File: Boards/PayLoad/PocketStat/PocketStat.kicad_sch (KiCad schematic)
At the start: 71 parts, among them J20 DX07S016JA1R1500, J3 MEM2061-01-188-00-A_REVA, J5 BM03B-SRSS-TBLFSN, Q1 BC857CMB_315, U1 HDC2080DMBR, U4 LPS22DFTR, U5 W25Q128JVSIQ TR, U6 BMP581, U8 ST1L05APU33R

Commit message: PocketStat update
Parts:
- removed R1, R2: 2k, Resistor-0402:RES_0402, symbol Device:R
- added R26, R27: 2k, Resistor-0402:RES_0402, symbol Device:R
- U4: footprint QFN_22DFTR_STM -> BARO LPS22DFTR:QFN_22DFTR_STM
- U6: footprint QFN10_BMP581_BOS -> BARO BMP581:QFN10_BMP581_BOS
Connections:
- net +3.3V: now also U4.6 (CS), R26.1, R27.1; no longer HM1.2 (~{CS})
- net BAR1 RDY: now also MCU2.2 (GPIO0); no longer MCU2.6 (GPIO4)
- net BAR2 RDY: now also MCU2.32 (GPIO21); no longer MCU2.15 (GPIO12)
- net GND: now also U4.5 (SDO/SA0), U6.5 (SDO); no longer HM1.5 (SDO)
- net Humidity RDY: now also MCU2.38 (GPIO26_ADC0); no longer MCU2.35 (GPIO23)
- net LED Status: now also MCU2.18 (GPIO15); no longer MCU2.31 (GPIO20)
- net MISO1 SPI: now also HM1.5 (SDO); no longer U4.5 (SDO/SA0), U6.5 (SDO)
- net MOSI1 SPI: now also HM1.3 (SDI); no longer U4.4 (SDA/SDI/SDISDO), U6.4 (SDI)
- net SCK1 SPI: now also HM1.4 (SCK); no longer U4.2 (SCK), U6.2 (SCK)
- net SCL0 I2C: now also U6.2 (SCK)
- net SCL1 I2C: now also U4.2 (SCK), R27.2; no longer HM1.4 (SCK)
- net SDA0 I2C: now also U6.4 (SDI)
- net SDA1 I2C: now also U4.4 (SDA/SDI/SDISDO), R26.2; no longer HM1.3 (SDI)
- net BAR1 ~{CS} SPI renamed HUM ~{CS} SPI
- net HUM ~{CS} SPI: now also HM1.2 (~{CS}); no longer U4.6 (CS)
- net BAR2 ~{CS} SPI: no longer names the net of U6.6 (CSB)
- net BAR2 ~{CS} SPI: no longer MCU2.16 (GPIO13)
- no-connect marks 19 -> 21
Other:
- note added: "BOSH BMP581: 400Hz, I2C ADDR 0x46 ST LPS22DF: 200Hz, I2C ADDR 0x5C"
- note added: "Bosh BME280: 1Hz Texas HDC2080: 1Hz, I2C ADDR 0x41"
- note removed: "Bosh BME280: 1Hz, I2C ADDR 0x76 Texas HDC2080: 1Hz, I2C ADDR 0x41"
- note removed: "ST LPS22DF 200Hz BOSH BMP581: 400Hz"
- moved on the sheet: C1, C13, C2, C28, C3, C4, C5, HM1, R17, R18, U1, U4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

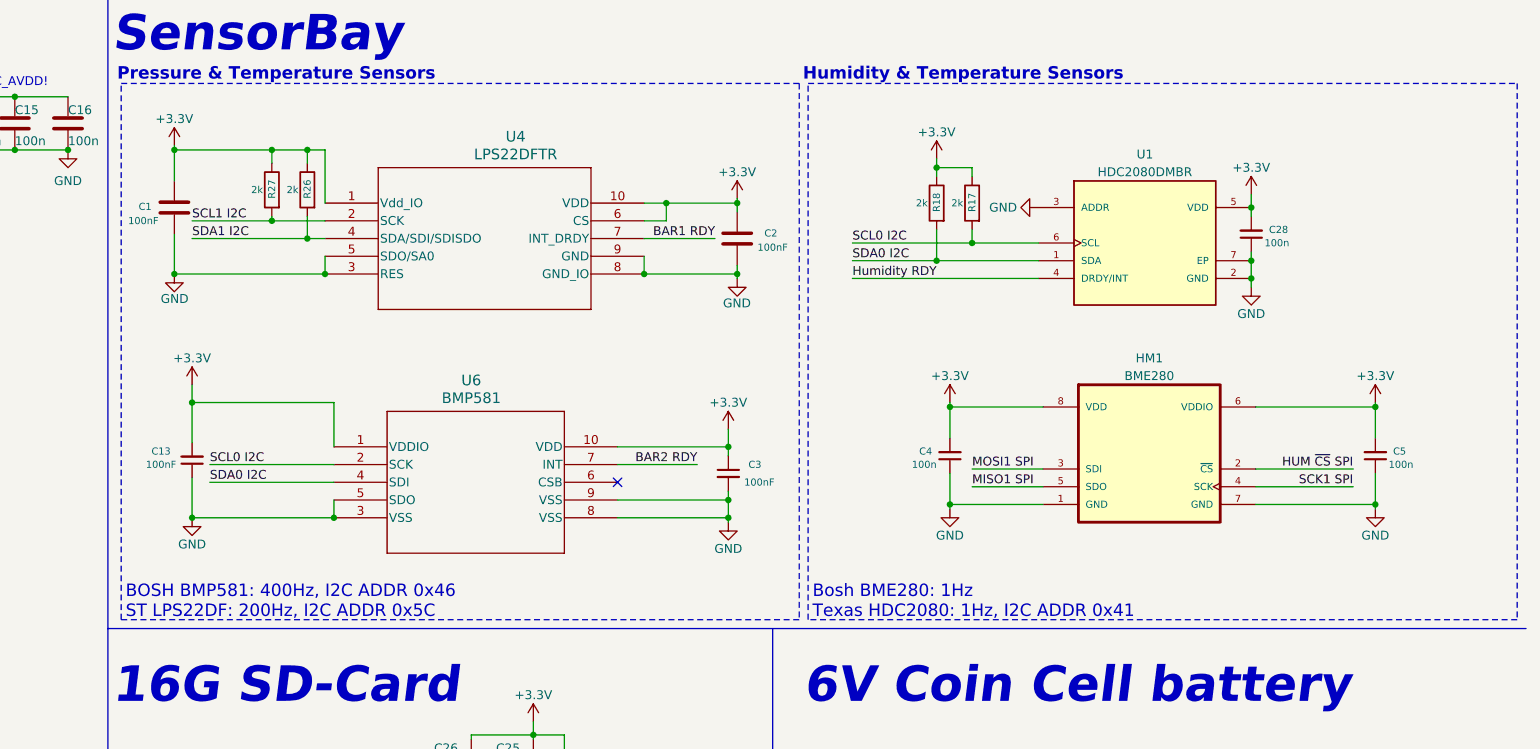
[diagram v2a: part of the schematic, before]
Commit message: Pocket Stat Schematic Notation Update
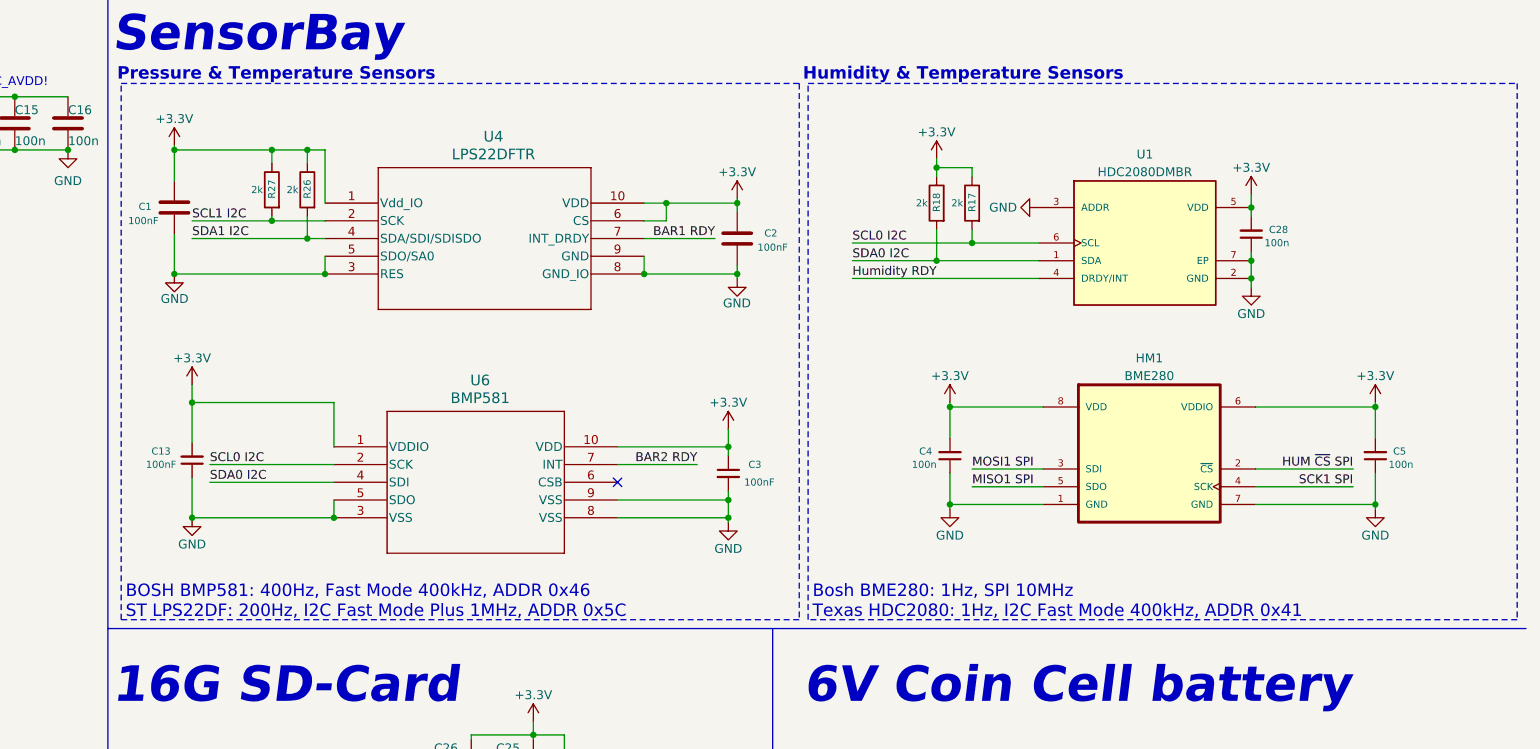
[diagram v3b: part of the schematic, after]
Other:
- note added: "BOSH BMP581: 400Hz, Fast Mode 400kHz, ADDR 0x46 ST LPS22DF: 200Hz, I2C Fast Mode Plus 1MHz, ADDR 0x5C"
- note added: "Bosh BME280: 1Hz, SPI 10MHz Texas HDC2080: 1Hz, I2C Fast Mode 400kHz, ADDR 0x41"
- note removed: "BOSH BMP581: 400Hz, I2C ADDR 0x46 ST LPS22DF: 200Hz, I2C ADDR 0x5C"
- note removed: "Bosh BME280: 1Hz Texas HDC2080: 1Hz, I2C ADDR 0x41"
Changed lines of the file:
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@@
 		)
 	)
-	(text "BOSH BMP581: 400Hz, I2C ADDR 0x46\nST LPS22DF: 200Hz, I2C ADDR 0x5C\n"
+	(text "BOSH BMP581: 400Hz, Fast Mode 400kHz, ADDR 0x46\nST LPS22DF: 200Hz, I2C Fast Mode Plus 1MHz, ADDR 0x5C\n"
 		(exclude_from_sim no)
 		(at 142.875 100.965 0)
@@
 		)
 	)
-	(text "Bosh BME280: 1Hz\nTexas HDC2080: 1Hz, I2C ADDR 0x41"
+	(text "Bosh BME280: 1Hz, SPI 10MHz\nTexas HDC2080: 1Hz, I2C Fast Mode 400kHz, ADDR 0x41"
 		(exclude_from_sim no)
 		(at 241.3 100.965 0)
@@
 		(dnp no)
 		(property "Reference" "U6"
-			(at 192.405 69.215 0)
+			(at 193.675 69.215 0)
 			(effects
 				(font
@@
 		)
 		(property "Value" "BMP581"
-			(at 192.405 71.755 0)
+			(at 193.675 71.755 0)
 			(effects
 				(font
@@
 		(dnp no)
 		(property "Reference" "U4"
-			(at 198.755 34.29 0)
+			(at 195.58 34.29 0)
 			(effects
 				(font
@@
 		)
 		(property "Value" "LPS22DFTR"
-			(at 198.755 36.83 0)
+			(at 195.58 36.83 0)
 			(effects
 				(font

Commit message: pocketstat power update
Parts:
- removed D1, D2: RSX301L-30DDTE25, Diode-Schottky_RSX301L:DIOM5026X220N, symbol RSX301L-30DDTE25:RSX301L-30DDTE25
- added D1, D2: PMEG2010ER, Diode-Schottky_PMEG2010ER:SODFL3517X110N, symbol PMEG2010ER:PMEG2010ER
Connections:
- net VBUS: now also D1.A
- net at JP6.1 (A): now also D2.A
- net +6V renamed +5V
- net +5V: now also D1.C, D2.C
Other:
- note added: "USB-C MUST BE DISCONNECTED WHEN BATTERY JUMPER IS SHORTED"
- moved on the sheet: BT1, C27, C36, C6, JP6

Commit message: update
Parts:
- C6: value 4.7u -> 1u
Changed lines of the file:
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@@
 			)
 		)
-		(property "Value" "4.7u"
+		(property "Value" "1u"
 			(at 262.89 144.78 0)
 			(effects

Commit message: PocketStat update
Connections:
- net SD-Card  ~{CS} SPI: now also D3.6 (IO4); no longer D3.3 (IO2)
- net SD-Card MISO SPI: now also D3.4 (IO3); no longer D3.1 (IO1)
- net SD-Card MOSI SPI: now also D3.3 (IO2); no longer D3.4 (IO3)
- net SD-Card SCK SPI: now also D3.1 (IO1); no longer D3.6 (IO4)
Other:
- moved on the sheet: D3
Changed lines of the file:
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@@
 	(wire
 		(pts
+			(xy 165.735 144.78) (xy 184.15 144.78)
+		)
+		(stroke
+			(width 0)
+			(type default)
+		)
+	)
+	(wire
+		(pts
 			(xy 74.93 48.895) (xy 77.47 48.895)
 		)
@@
 	(wire
 		(pts
+			(xy 165.735 147.32) (xy 184.15 147.32)
+		)
+		(stroke
+			(width 0)
+			(type default)
+		)
+	)
+	(wire
+		(pts
 			(xy 225.425 247.65) (xy 227.965 247.65)
 		)
@@
 	(wire
 		(pts
-			(xy 177.8 142.24) (xy 177.8 147.32)
+			(xy 165.735 142.24) (xy 184.15 142.24)
 		)
 		(stroke
@@
 	(wire
 		(pts
-			(xy 180.34 144.78) (xy 205.74 144.78)
+			(xy 150.495 250.19) (xy 150.495 251.46)
 		)
 		(stroke
@@
 	(wire
 		(pts
-			(xy 150.495 250.19) (xy 150.495 251.46)
+			(xy 40.64 112.395) (xy 46.99 112.395)
 		)
 		(stroke
@@
 	(wire
 		(pts
-			(xy 40.64 112.395) (xy 46.99 112.395)
+			(xy 201.295 126.365) (xy 201.295 125.73)
 		)
 		(stroke
@@
 	(wire
 		(pts
-			(xy 201.295 126.365) (xy 201.295 125.73)
+			(xy 187.325 142.24) (xy 205.74 142.24)
 		)
 		(stroke
@@
 	(wire
 		(pts
-			(xy 175.26 139.7) (xy 180.34 139.7)
-		)
-		(stroke
-			(width 0)
-			(type default)
-		)
-	)
-	(wire
-		(pts
 			(xy 265.43 223.52) (xy 266.7 223.52)
 		)
@@
 	(wire
 		(pts
-			(xy 153.67 142.24) (xy 153.67 144.145)
-		)
-		(stroke
-			(width 0)
-			(type default)
-		)
-	)
-	(wire
-		(pts
-			(xy 182.245 137.16) (xy 182.245 142.24)
+			(xy 144.145 147.32) (xy 144.145 149.225)
 		)
 		(stroke
@@
 	(wire
 		(pts
-			(xy 182.245 142.24) (xy 205.74 142.24)
-		)
-		(stroke
-			(width 0)
-			(type default)
-		)
-	)
-	(wire
-		(pts
 			(xy 171.45 36.195) (xy 171.45 43.815)
 		)
@@
 	(wire
 		(pts
+			(xy 187.325 147.32) (xy 205.74 147.32)
+		)
+		(stroke
+			(width 0)
+			(type default)
+		)
+	)
+	(wire
+		(pts
 			(xy 57.15 36.195) (xy 64.77 36.195)
 		)
@@
 	(wire
 		(pts
-			(xy 180.34 139.7) (xy 180.34 144.78)
-		)
-		(stroke
-			(width 0)
-			(type default)
-		)
-	)
-	(wire
-		(pts
 			(xy 92.71 28.575) (xy 85.09 28.575)
 		)
@@
 	(wire
 		(pts
-			(xy 175.26 137.16) (xy 182.245 137.16)
-		)
-		(stroke
-			(width 0)
-			(type default)
-		)
-	)
-	(wire
-		(pts
 			(xy 44.45 38.1) (xy 44.45 46.355)
 		)
@@
 	(wire
 		(pts
+			(xy 187.325 134.62) (xy 205.74 134.62)
+		)
+		(stroke
+			(width 0)
+			(type default)
+		)
+	)
+	(wire
+		(pts
 			(xy 97.79 125.095) (xy 116.205 125.095)
 		)
@@
 	(wire
 		(pts
-			(xy 175.26 142.24) (xy 177.8 142.24)
-		)
-		(stroke
-			(width 0)
-			(type default)
-		)
-	)
-	(wire
-		(pts
 			(xy 155.575 205.105) (xy 155.575 206.375)
 		)
@@
 	(wire
 		(pts
-			(xy 175.26 134.62) (xy 205.74 134.62)
-		)
-		(stroke
-			(width 0)
-			(type default)
-		)
-	)
-	(wire
-		(pts
 			(xy 133.35 160.655) (xy 133.35 161.29)
 		)
@@
 	(wire
 		(pts
-			(xy 153.67 132.08) (xy 153.67 134.62)
+			(xy 144.145 137.16) (xy 144.145 139.7)
 		)
 		(stroke
@@
 	(wire
 		(pts
-			(xy 177.8 147.32) (xy 205.74 147.32)
+			(xy 300.355 212.09) (xy 300.355 214.63)
 		)
 		(stroke
@@
 	(wire
 		(pts
-			(xy 300.355 212.09) (xy 300.355 214.63)
+			(xy 120.65 231.14) (xy 135.89 231.14)
 		)
 		(stroke
@@
 	(wire
 		(pts
-			(xy 120.65 231.14) (xy 135.89 231.14)
+			(xy 220.345 46.355) (xy 220.345 43.815)
 		)
 		(stroke
@@
 		)
 	)
-	(wire
+	(polyline
 		(pts
-			(xy 220.345 46.355) (xy 220.345 43.815)
+			(xy 235.585 104.775) (xy 235.585 248.285)
 		)
 		(stroke
@@
 		)
 	)
-	(polyline
+	(wire
 		(pts
-			(xy 235.585 104.775) (xy 235.585 248.285)
+			(xy 230.505 43.815) (xy 230.505 45.085)
 		)
 		(stroke
@@
 	(wire
 		(pts
-			(xy 230.505 43.815) (xy 230.505 45.085)
+			(xy 165.735 139.7) (xy 184.15 139.7)
 		)
 		(stroke
@@
 	(wire
 		(pts
+			(xy 187.325 144.78) (xy 205.74 144.78)
+		)
+		(stroke
+			(width 0)
+			(type default)
+		)
+	)
+	(wire
+		(pts
 			(xy 149.86 36.195) (xy 149.86 40.64)
 		)
@@
 		)
 	)
+	(label "SD-Card SCK SPI"
+		(at 184.15 139.7 180)
+		(effects
+			(font
+				(size 1.27 1.27)
+			)
+			(justify right bottom)
+		)
+	)
 	(label "SCL0 I2C"
 		(at 116.205 120.015 180)
@@
 		)
 	)
+	(label "SD-Card MOSI SPI"
+		(at 184.15 142.24 180)
+		(effects
+			(font
+				(size 1.27 1.27)
+			)
+			(justify right bottom)
+		)
+	)
 	(label "MOSI1 SPI"
 		(at 116.205 84.455 180)
@@
 	)
 	(label "SD-Card MISO SPI"
+		(at 184.15 144.78 180)
+		(effects
+			(font
+				(size 1.27 1.27)
+			)
+			(justify right bottom)
+		)
+	)
+	(label "SD-Card MISO SPI"
 		(at 187.325 134.62 0)
 		(effects
@@
 		)
 	)
+	(label "SD-Card  ~{CS} SPI"
+		(at 184.15 147.32 180)
+		(effects
+			(font
+				(size 1.27 1.27)
+			)
+			(justify right bottom)
+		)
+	)
 	(label "MCU SCLK SPI"
 		(at 31.75 89.535 0)
@@
 	(symbol
 		(lib_id "power:GND")
-		(at 153.67 144.145 0)
+		(at 144.145 149.225 0)
 		(unit 1)
 		(exclude_from_sim no)
@@
 		(dnp no)
 		(property "Reference" "#PWR018"
-			(at 153.67 150.495 0)
+			(at 144.145 155.575 0)
 			(effects
 				(font
@@
 		)
 		(property "Value" "GND"
-			(at 153.67 147.955 0)
+			(at 144.145 153.035 0)
 			(effects
 				(font
@@
 		)
 		(property "Footprint" ""
-			(at 153.67 144.145 0)
+			(at 144.145 149.225 0)
 			(effects
 				(font
@@
 		)
 		(property "Datasheet" ""
-			(at 153.67 144.145 0)
+			(at 144.145 149.225 0)
 			(effects
 				(font
@@
 		)
 		(property "Description" "Power symbol creates a global label with name \"GND\" , ground"
-			(at 153.67 144.145 0)
+			(at 144.145 149.225 0)
 			(effects
 				(font
@@
 	(symbol
 		(lib_id "power:+3.3V")
-		(at 153.67 132.08 0)
+		(at 144.145 137.16 0)
 		(unit 1)
 		(exclude_from_sim no)
@@
 		(dnp no)
 		(property "Reference" "#PWR017"
-			(at 153.67 135.89 0)
+			(at 144.145 140.97 0)
 			(effects
 				(font
@@
 		)
 		(property "Value" "+3.3V"
-			(at 153.67 128.27 0)
+			(at 144.145 133.35 0)
 			(effects
 				(font
@@
 		)
 		(property "Footprint" ""
-			(at 153.67 132.08 0)
+			(at 144.145 137.16 0)
 			(effects
 				(font
@@
 		)
 		(property "Datasheet" ""
-			(at 153.67 132.08 0)
+			(at 144.145 137.16 0)
 			(effects
 				(font
@@
 		)
 		(property "Description" "Power symbol creates a global label with name \"+3.3V\""
-			(at 153.67 132.08 0)
+			(at 144.145 137.16 0)
 			(effects
 				(font
@@
 	(symbol
 		(lib_id "SP3004-04XTG:SP3004-04XTG")
-		(at 175.26 134.62 0)
+		(at 165.735 139.7 0)
 		(mirror y)
 		(unit 1)
@@
 		(dnp no)
 		(property "Reference" "D3"
-			(at 163.83 128.905 0)
+			(at 154.305 133.985 0)
 			(effects
 				(font
@@
 		)
 		(property "Value" "SP3004-04XTG"
-			(at 163.83 131.445 0)
+			(at 154.305 136.525 0)
 			(effects
 				(font
@@
 		)
 		(property "Footprint" "TVS-SP3004:SOT563_LTF"
-			(at 148.59 229.54 0)
+			(at 139.065 234.62 0)
 			(effects
 				(font
@@
 		)
 		(property "Datasheet" "https://m.littelfuse.com/~/media/electronics/datasheets/tvs_diode_arrays/littelfuse_tvs_diode_array_sp3004_datasheet.pdf.pdf"
-			(at 148.59 329.54 0)
+			(at 139.065 334.62 0)
 			(effects
 				(font
@@
 		)
 		(property "Description" "LITTELFUSE - SP3004-04XTG - TVS Diode, Unidirectional, 6 V, 15 V, SOT-563, 6 Pins"
-			(at 175.26 134.62 0)
+			(at 165.735 139.7 0)
 			(effects
 				(font
@@
 		)
 		(property "Height" "0.6"
-			(at 148.59 529.54 0)
+			(at 139.065 534.62 0)
 			(effects
 				(font
@@
 		)
 		(property "Mouser Part Number" "576-SP3004-04XTG"
-			(at 148.59 629.54 0)
+			(at 139.065 634.62 0)
 			(effects
 				(font
@@
 		)
 		(property "Mouser Price/Stock" "https://www.mouser.co.uk/ProductDetail/Littelfuse/SP3004-04XTG?qs=trbuaetfxXQ7JjseAkJ3Ww%3D%3D"
-			(at 148.59 729.54 0)
+			(at 139.065 734.62 0)
 			(effects
 				(font
@@
 		)
 		(property "Manufacturer_Name" "LITTELFUSE"
-			(at 148.59 829.54 0)
+			(at 139.065 834.62 0)
 			(effects
 				(font
@@
 		)
 		(property "Manufacturer_Part_Number" "SP3004-04XTG"
-			(at 148.59 929.54 0)
+			(at 139.065 934.62 0)
 			(effects
 				(font

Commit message: PocketSat
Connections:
- net MCU ~{BOOT} renamed MCU ~{RST}
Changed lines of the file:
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@@
 		)
 	)
-	(label "MCU ~{BOOT}"
+	(label "MCU ~{RST}"
 		(at 44.45 38.1 180)
 		(effects

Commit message: PocketSat Finished
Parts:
- H1, H2, H3, H4: footprint MountingHole:MountingHole_2.2mm_M2_ISO7380_Pad_TopBottom -> MountingHole:MountingHole_2.2mm_M2_ISO7380
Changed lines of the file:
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@@
 			)
 		)
-		(property "Footprint" "MountingHole:MountingHole_2.2mm_M2_ISO7380_Pad_TopBottom"
+		(property "Footprint" "MountingHole:MountingHole_2.2mm_M2_ISO7380"
 			(at 38.1 165.735 0)
 			(effects
@@
 			)
 		)
-		(property "Footprint" "MountingHole:MountingHole_2.2mm_M2_ISO7380_Pad_TopBottom"
+		(property "Footprint" "MountingHole:MountingHole_2.2mm_M2_ISO7380"
 			(at 17.78 165.1 0)
 			(effects
@@
 			)
 		)
-		(property "Footprint" "MountingHole:MountingHole_2.2mm_M2_ISO7380_Pad_TopBottom"
+		(property "Footprint" "MountingHole:MountingHole_2.2mm_M2_ISO7380"
 			(at 38.1 158.75 0)
 			(effects
@@
 			)
 		)
-		(property "Footprint" "MountingHole:MountingHole_2.2mm_M2_ISO7380_Pad_TopBottom"
+		(property "Footprint" "MountingHole:MountingHole_2.2mm_M2_ISO7380"
 			(at 17.78 158.75 0)
 			(effects
